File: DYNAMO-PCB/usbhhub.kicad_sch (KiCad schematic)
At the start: 2 parts, among them U1 TPS65988DHRSHR, U3 USB7206/KDX

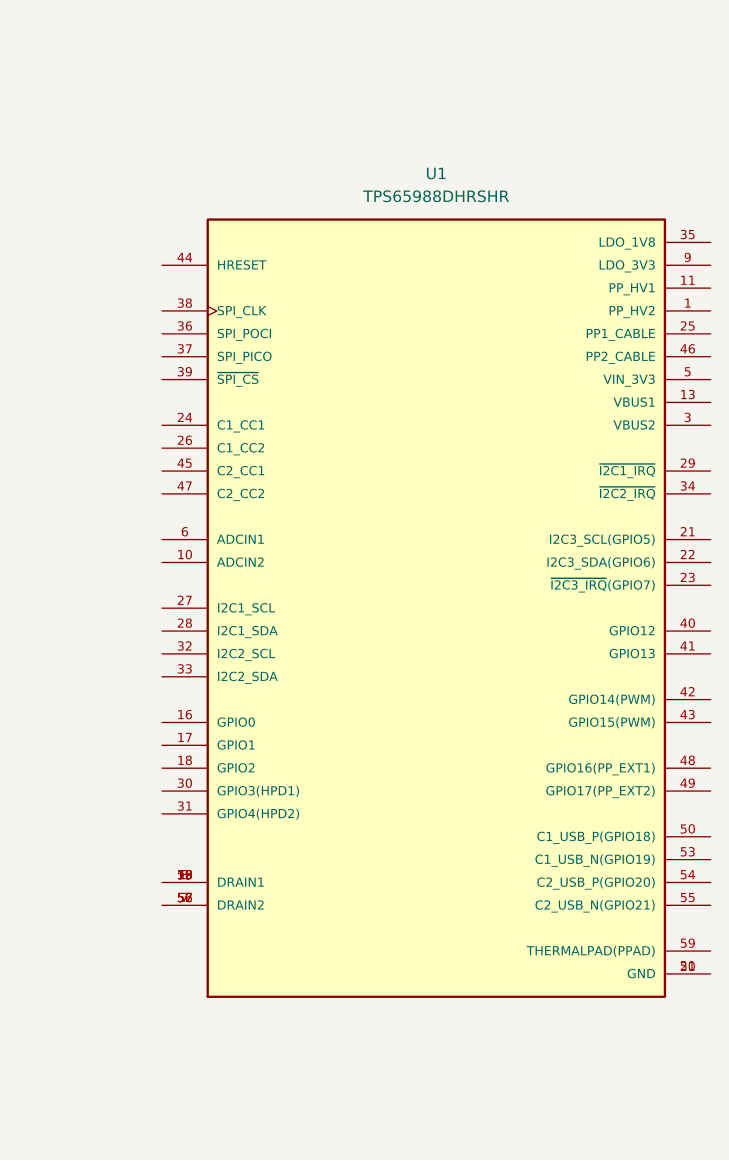
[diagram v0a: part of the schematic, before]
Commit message: removed unncessary ic
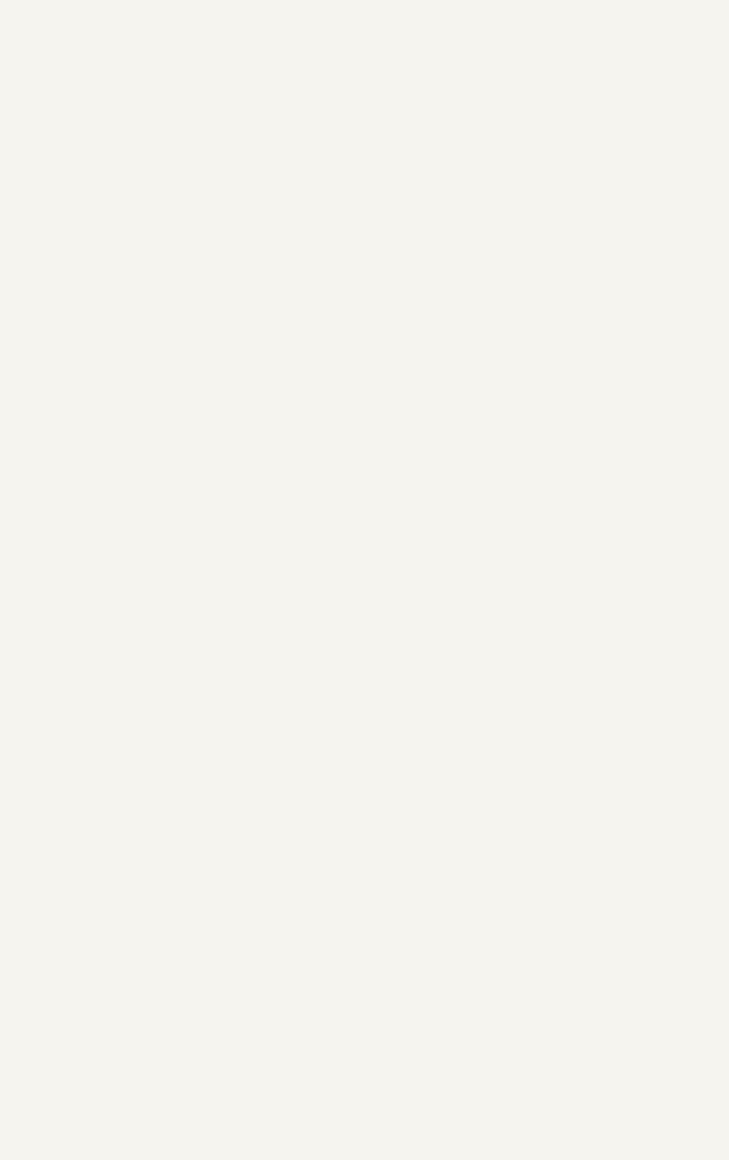
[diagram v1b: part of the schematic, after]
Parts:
- removed U1: TPS65988DHRSHR, TPS65988DHRSHR:IC_TPS65987DDHRSHR, symbol TPS65988DHRSHR:TPS65988DHRSHR
